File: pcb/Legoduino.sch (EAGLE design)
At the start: 91 parts, among them CON11 ISP-AVR, CON2 PIN(1+16)X3_DS, IC1 NCP3170ADR2G, IC2 RN-42, IC3 MIC5205-5.0YM5, IC4 ATMEGA2560-16AU, IC5 UG-2864HSWEG01_SPI, IC6 MIC5205-3.6YM5, IC7 MIC5205-3.3YM5, IC8 BD6221F-E2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

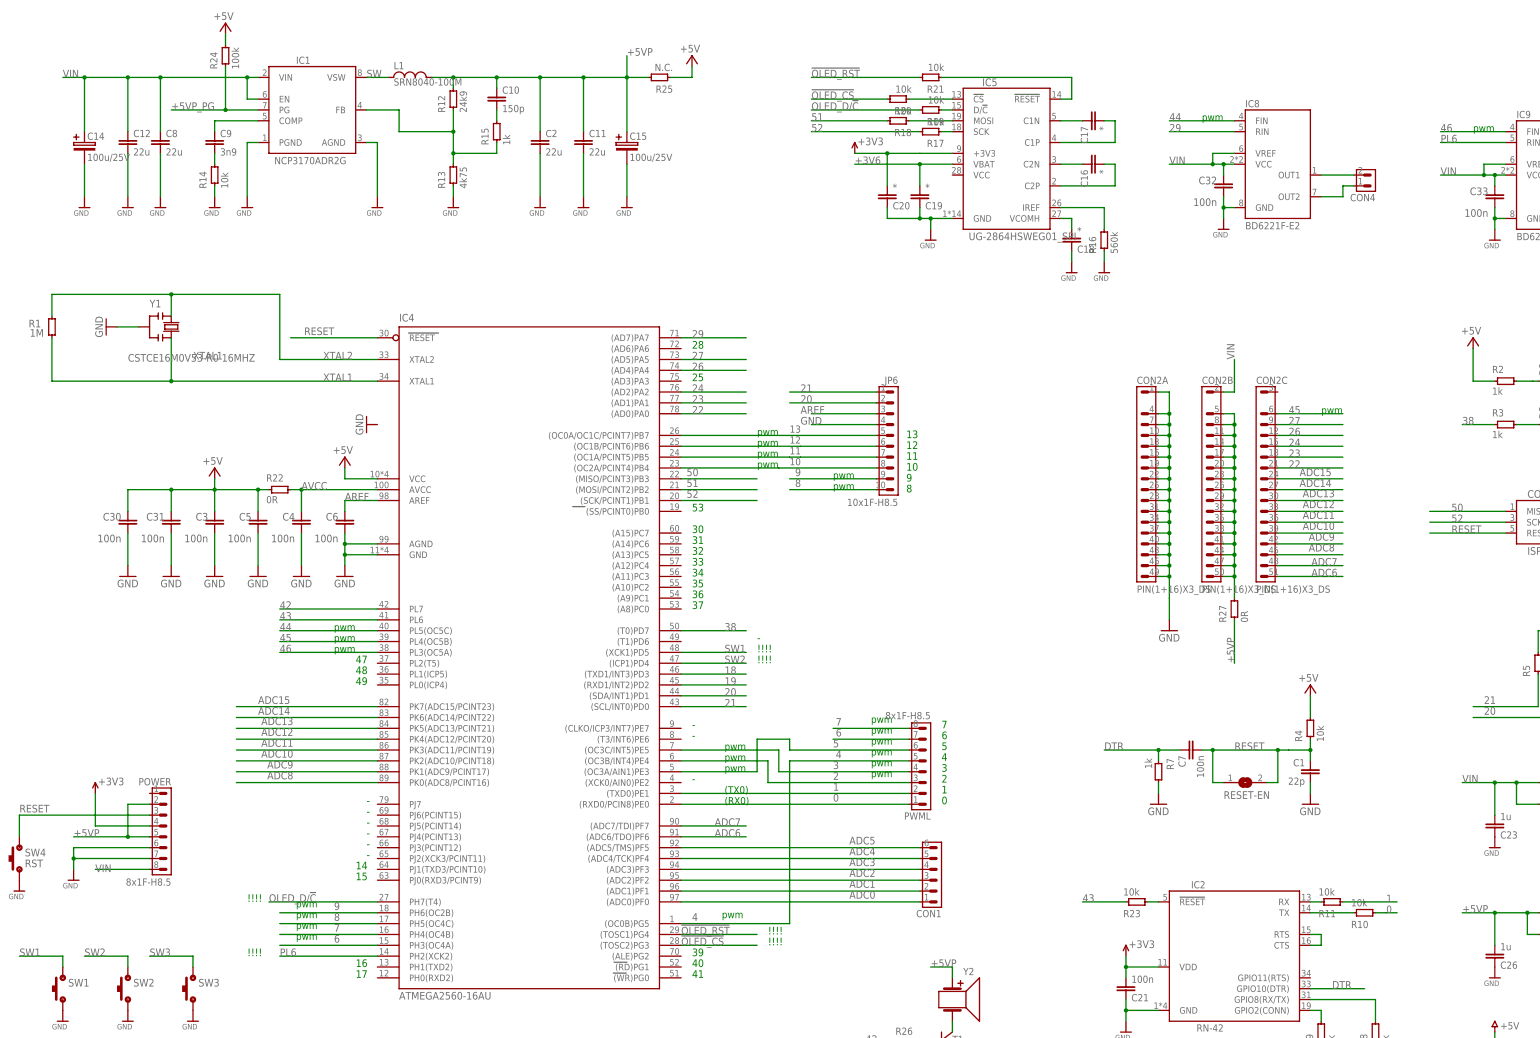
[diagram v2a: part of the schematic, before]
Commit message: Updated net names according to Arduino Mega pin numbers
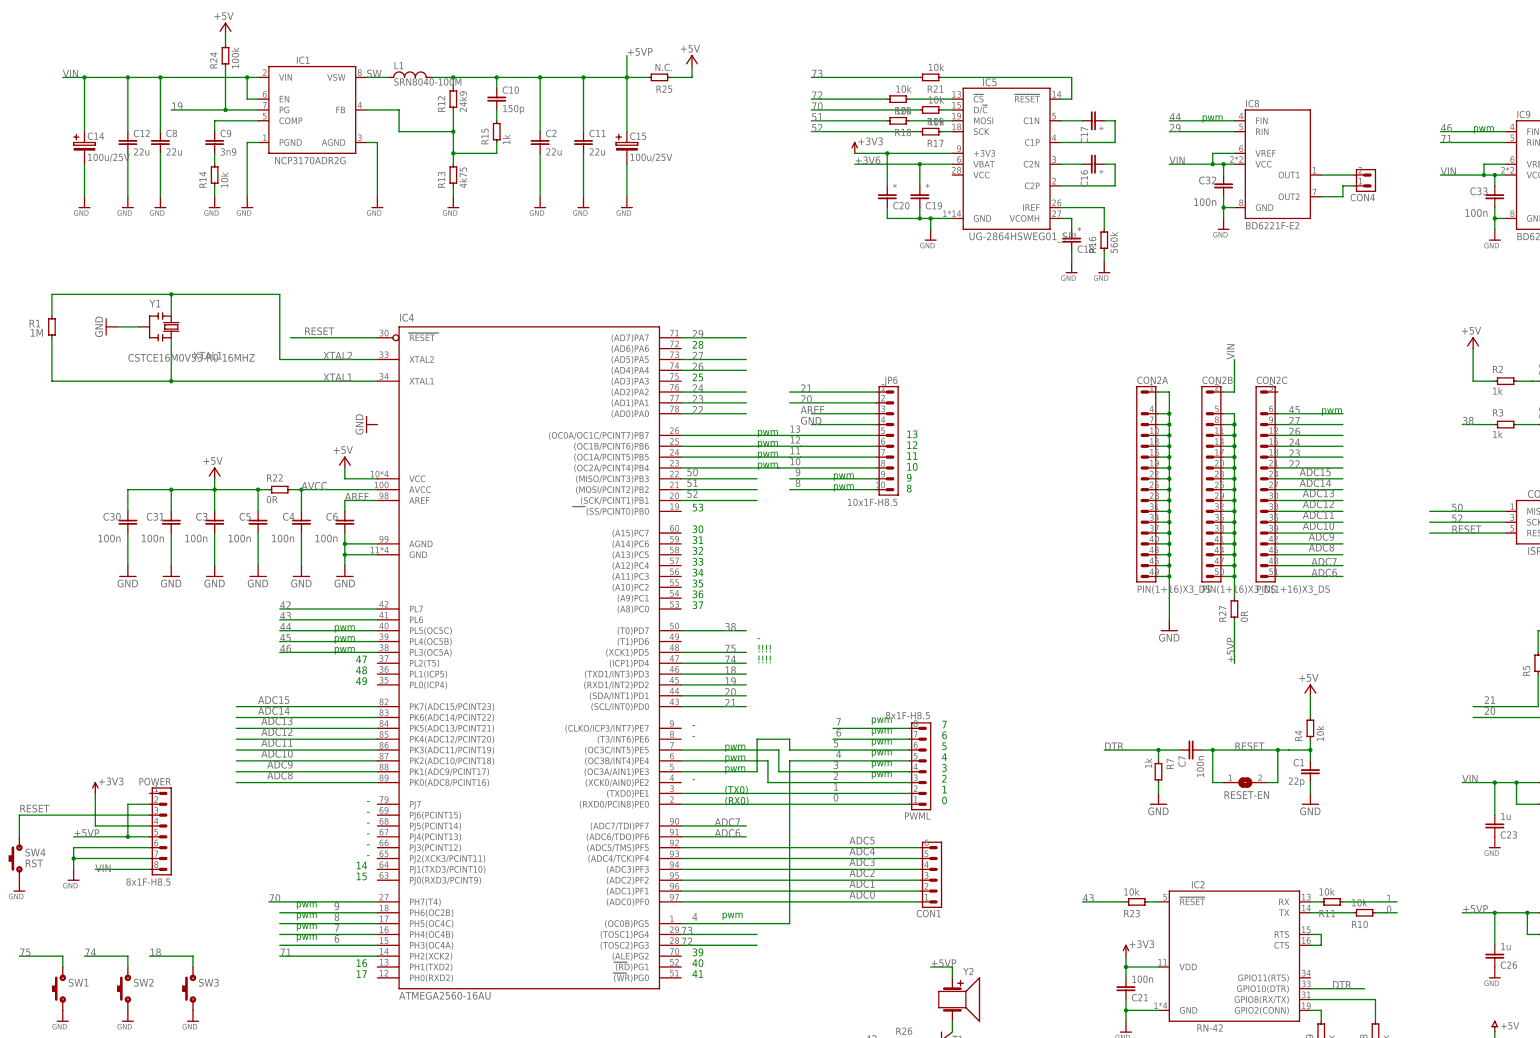
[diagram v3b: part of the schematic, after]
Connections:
- net !OLED_CS renamed 72
- net !OLED_RST renamed 73
- net OLED_D/!C renamed 70
- net PL6 renamed 71
- net SW1 renamed 75
- net SW2 renamed 74
- removed net +5VP_PG: IC1.PG, R24.1
- removed net SW3: SW3.1
- net 18: now also SW3.1
- net 19: now also IC1.PG, R24.1
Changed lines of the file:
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@@
 <text x="114.3" y="101.6" size="1.778" layer="91">14</text>
 <text x="114.3" y="99.06" size="1.778" layer="91">15</text>
-<text x="88.9" y="93.98" size="1.778" layer="91">!!!!</text>
-<text x="88.9" y="81.28" size="1.778" layer="91">!!!!</text>
 <text x="114.3" y="78.74" size="1.778" layer="91">16</text>
 <text x="114.3" y="76.2" size="1.778" layer="91">17</text>
 <text x="193.04" y="81.28" size="1.778" layer="91">39</text>
-<text x="210.82" y="86.36" size="1.778" layer="91">!!!!</text>
-<text x="210.82" y="83.82" size="1.778" layer="91">!!!!</text>
 <text x="193.04" y="78.74" size="1.778" layer="91">40</text>
 <text x="193.04" y="76.2" size="1.778" layer="91">41</text>
@@
 </segment>
 </net>
-<net name="OLED_D/!C" class="0">
+<net name="70" class="0">
 <segment>
 <label x="220.98" y="279.4" size="1.778" layer="95"/>
@@
 </segment>
 </net>
-<net name="!OLED_CS" class="0">
+<net name="72" class="0">
 <segment>
 <label x="220.98" y="281.94" size="1.778" layer="95"/>
@@
 </segment>
 </net>
-<net name="!OLED_RST" class="0">
+<net name="73" class="0">
 <segment>
 <pinref part="R21" gate="G$1" pin="2"/>
@@
 </segment>
 </net>
-<net name="+5VP_PG" class="0">
-<segment>
-<pinref part="IC1" gate="G$1" pin="PG"/>
-<wire x1="91.44" y1="279.4" x2="83.82" y2="279.4" width="0.1524" layer="91"/>
-<label x="71.12" y="279.4" size="1.778" layer="95"/>
-<pinref part="R24" gate="G$1" pin="1"/>
-<wire x1="83.82" y1="279.4" x2="71.12" y2="279.4" width="0.1524" layer="91"/>
-<wire x1="83.82" y1="289.56" x2="83.82" y2="279.4" width="0.1524" layer="91"/>
-<junction x="83.82" y="279.4"/>
-</segment>
-</net>
 <net name="N$29" class="0">
 <segment>
@@
 </segment>
 </net>
-<net name="PL6" class="0">
+<net name="71" class="0">
 <segment>
 <pinref part="IC4" gate="1" pin="PH2(XCK2)"/>
@@
 </segment>
 </net>
-<net name="SW1" class="0">
+<net name="75" class="0">
 <segment>
 <pinref part="SW1" gate="G$1" pin="1"/>
@@
 </segment>
 </net>
-<net name="SW2" class="0">
+<net name="74" class="0">
 <segment>
 <pinref part="SW2" gate="G$1" pin="1"/>
@@
 <label x="200.66" y="149.86" size="1.778" layer="95"/>
 <pinref part="IC4" gate="1" pin="(ICP1)PD4"/>
-</segment>
-</net>
-<net name="SW3" class="0">
-<segment>
-<pinref part="SW3" gate="G$1" pin="1"/>
-<wire x1="76.2" y1="78.74" x2="76.2" y2="81.28" width="0.1524" layer="91"/>
-<wire x1="76.2" y1="81.28" x2="66.04" y2="81.28" width="0.1524" layer="91"/>
-<label x="66.04" y="81.28" size="1.778" layer="95"/>
 </segment>
 </net>
@@
 <pinref part="IC4" gate="1" pin="(RXD1/INT2)PD2"/>
 </segment>
+<segment>
+<pinref part="IC1" gate="G$1" pin="PG"/>
+<wire x1="91.44" y1="279.4" x2="83.82" y2="279.4" width="0.1524" layer="91"/>
+<label x="71.12" y="279.4" size="1.778" layer="95"/>
+<pinref part="R24" gate="G$1" pin="1"/>
+<wire x1="83.82" y1="279.4" x2="71.12" y2="279.4" width="0.1524" layer="91"/>
+<wire x1="83.82" y1="289.56" x2="83.82" y2="279.4" width="0.1524" layer="91"/>
+<junction x="83.82" y="279.4"/>
+</segment>
 </net>
 <net name="18" class="0">
@@
 <pinref part="IC4" gate="1" pin="(TXD1/INT3)PD3"/>
 </segment>
-</net>
+<segment>
+<pinref part="SW3" gate="G$1" pin="1"/>
+<wire x1="76.2" y1="78.74" x2="76.2" y2="81.28" width="0.1524" layer="91"/>
+<wire x1="76.2" y1="81.28" x2="66.04" y2="81.28" width="0.1524" layer="91"/>
+<label x="66.04" y="81.28" size="1.778" layer="95"/>
+</segment>
+</net>

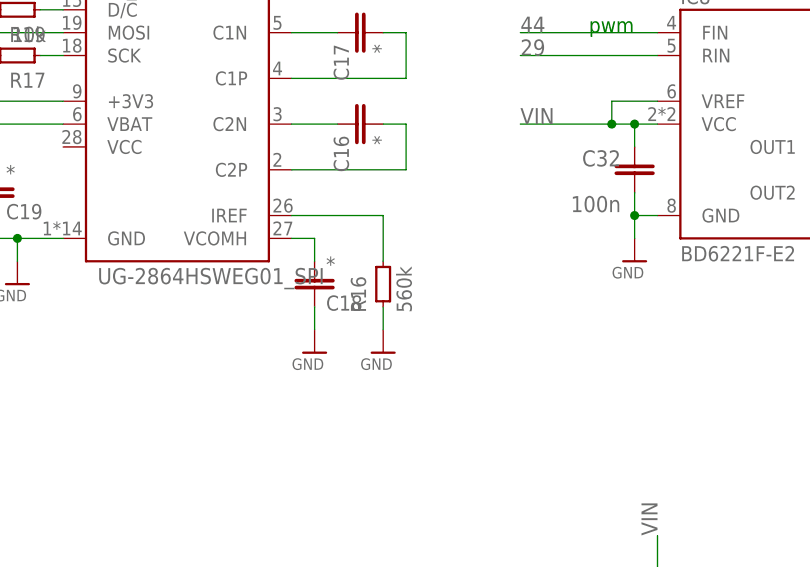
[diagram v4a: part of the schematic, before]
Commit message: R16 -> 390k. Closes #32.
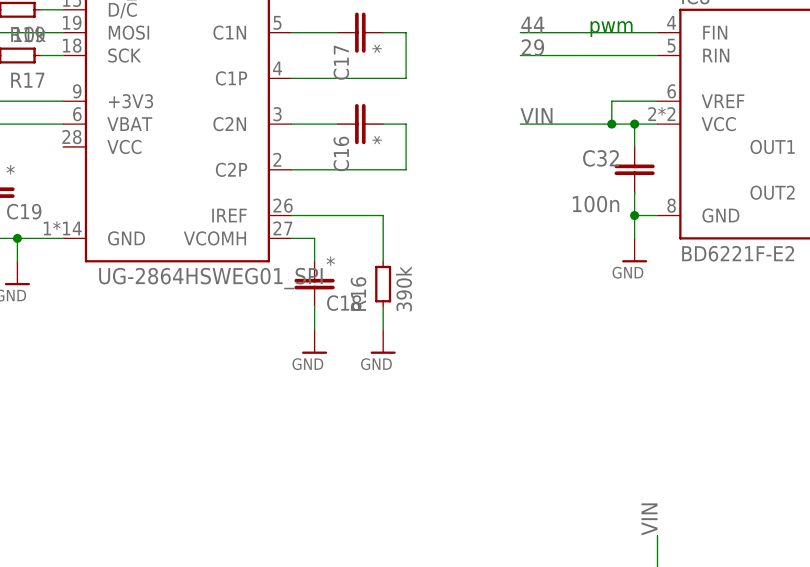
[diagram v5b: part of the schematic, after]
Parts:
- R16: value 560k -> 390k
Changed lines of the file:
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@@
 <part name="C18" library="PN_default" deviceset="C" device="0603" value="*"/>
 <part name="GND26" library="PN_default" deviceset="GND" device=""/>
-<part name="R16" library="PN_default" deviceset="R" device="0603" value="560k"/>
+<part name="R16" library="PN_default" deviceset="R" device="0603" value="390k"/>
 <part name="GND27" library="PN_default" deviceset="GND" device=""/>
 <part name="IC5" library="PN_opto" deviceset="UG-2864HSWEG01_SPI" device=""/>

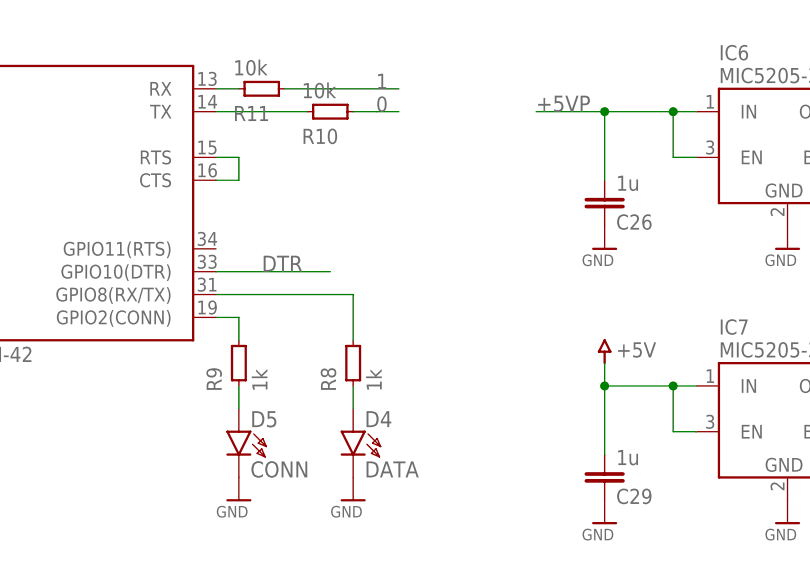
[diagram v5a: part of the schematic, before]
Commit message: Reverse DATA LED polarisation. Closes #15.
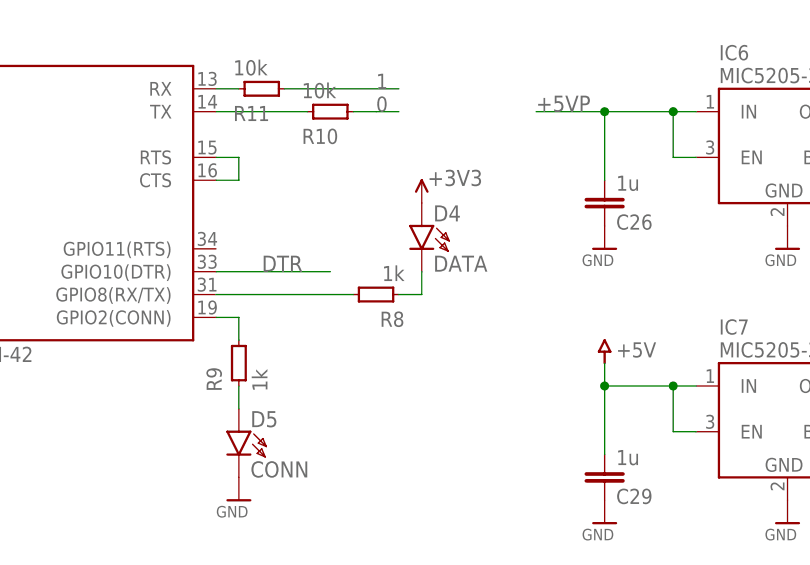
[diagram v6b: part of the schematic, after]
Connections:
- net +3V3: now also D4.A
- net GND: no longer D4.K
- net N$6: now also D4.K; no longer D4.A
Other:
- moved on the sheet: D4, R8
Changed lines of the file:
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@@
 <part name="D4" library="PN_default" deviceset="LED" device="0805" value="DATA"/>
 <part name="D5" library="PN_default" deviceset="LED" device="0805" value="CONN"/>
-<part name="GND3" library="PN_default" deviceset="GND" device=""/>
 <part name="GND4" library="PN_default" deviceset="GND" device=""/>
 <part name="IC4" library="PN_microcontrollers" deviceset="ATMEGA2560" device="AU" technology="-16"/>
@@
 <part name="P+6" library="supply1" deviceset="+5V" device=""/>
 <part name="R27" library="PN_default" deviceset="R" device="0805" value="0R"/>
+<part name="U$4" library="PN_default" deviceset="+3V3" device=""/>
 </parts>
 <sheets>
@@
 <instance part="R6" gate="G$1" x="398.78" y="149.86" rot="R90"/>
 <instance part="R7" gate="G$1" x="302.26" y="124.46" rot="R270"/>
-<instance part="R8" gate="G$1" x="353.06" y="63.5" rot="R90"/>
+<instance part="R8" gate="G$1" x="355.6" y="71.12" rot="R180"/>
 <instance part="R9" gate="G$1" x="340.36" y="63.5" rot="R90"/>
 <instance part="R10" gate="G$1" x="350.52" y="91.44" rot="MR180"/>
@@
 <instance part="D2" gate="G$1" x="396.24" y="215.9" rot="R90"/>
 <instance part="D3" gate="G$1" x="396.24" y="205.74" rot="R90"/>
-<instance part="D4" gate="G$1" x="353.06" y="53.34"/>
+<instance part="D4" gate="G$1" x="360.68" y="76.2"/>
 <instance part="D5" gate="G$1" x="340.36" y="53.34"/>
-<instance part="GND3" gate="G$1" x="353.06" y="48.26"/>
 <instance part="GND4" gate="G$1" x="340.36" y="48.26"/>
 <instance part="IC4" gate="1" x="154.94" y="149.86"/>
@@
 </instance>
 <instance part="R27" gate="G$1" x="320.04" y="162.56" rot="R90"/>
+<instance part="U$4" gate="G$1" x="360.68" y="83.82"/>
 </instances>
 <busses>
@@
 <pinref part="GND4" gate="G$1" pin="GND"/>
 <pinref part="D5" gate="G$1" pin="K"/>
-</segment>
-<segment>
-<pinref part="GND3" gate="G$1" pin="GND"/>
-<pinref part="D4" gate="G$1" pin="K"/>
 </segment>
 <segment>
@@
 <junction x="426.72" y="60.96"/>
 </segment>
+<segment>
+<pinref part="D4" gate="G$1" pin="A"/>
+<pinref part="U$4" gate="G$1" pin="+3V3"/>
+</segment>
 </net>
 <net name="20" class="0">
@@
 <segment>
 <pinref part="R8" gate="G$1" pin="2"/>
-<wire x1="353.06" y1="66.04" x2="353.06" y2="71.12" width="0.1524" layer="91"/>
 <wire x1="353.06" y1="71.12" x2="337.82" y2="71.12" width="0.1524" layer="91"/>
 <pinref part="IC2" gate="G$1" pin="GPIO8(RX/TX)"/>
-</segment>
-</net>
-<net name="N$6" class="0">
-<segment>
-<pinref part="D4" gate="G$1" pin="A"/>
-<pinref part="R8" gate="G$1" pin="1"/>
-<wire x1="353.06" y1="60.96" x2="353.06" y2="58.42" width="0.1524" layer="91"/>
 </segment>
 </net>
@@
 </segment>
 </net>
+<net name="N$6" class="0">
+<segment>
+<pinref part="R8" gate="G$1" pin="1"/>
+<pinref part="D4" gate="G$1" pin="K"/>
+<wire x1="358.14" y1="71.12" x2="360.68" y2="71.12" width="0.1524" layer="91"/>
+<wire x1="360.68" y1="71.12" x2="360.68" y2="73.66" width="0.1524" layer="91"/>
+</segment>
+</net>

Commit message: #20: Optimized pin assignment on arduino shield connector. PWM signals are now connected only to this lines, where PWM are on Arduino Uno board. 4 additional PWM are now connected to expansion connector. 2 are reserved to connect to OC transistors.
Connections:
- removed net 45: CON2C.2, IC4.PL4(OC5B)
- new net 25: CON2C.5, IC4.(OC3A/AIN1)PE3
- new net 28: CON2C.2, IC4.PL3(OC5A)
- new net OC_PWM1: IC4.PH3(OC4A)
- new net OC_PWM2: IC4.PL4(OC5B)
- net 10: now also IC4.(OC1B/PCINT6)PB6; no longer IC4.(OC2A/PCINT4)PB4
- net 11: now also IC4.(OC0A/OC1C/PCINT7)PB7; no longer IC4.(OC1A/PCINT5)PB5
- net 12: no longer IC4.(OC1B/PCINT6)PB6
- net 13: no longer IC4.(OC0A/OC1C/PCINT7)PB7
- net 2: now also IC4.PH0(RXD2); no longer IC4.(OC3B/INT4)PE4
- net 22: no longer CON2C.7
- net 23: now also CON2C.7; no longer CON2C.6
- net 24: now also CON2C.6, IC4.(OC0B)PG5; no longer CON2C.5, IC4.(AD2)PA2
- net 26: now also IC4.(OC3B/INT4)PE4; no longer IC4.(AD4)PA4
- net 27: now also IC4.(OC3C/INT5)PE5; no longer IC4.(AD5)PA5
- net 3: now also IC4.PH4(OC4B); no longer IC4.(OC3C/INT5)PE5
- net 4: now also IC4.PH1(TXD2); no longer IC4.(OC0B)PG5
- net 46: now also IC4.(OC2A/PCINT4)PB4; no longer IC4.PL3(OC5A)
- net 5: now also IC4.PH5(OC4C); no longer IC4.(OC3A/AIN1)PE3
- net 6: now also IC4.PH6(OC2B); no longer IC4.PH3(OC4A)
- net 7: now also IC4.PH2(XCK2); no longer IC4.PH4(OC4B)
- net 71: now also IC4.(SS/PCINT0)PB0; no longer IC4.PH2(XCK2)
- net 8: no longer IC4.PH5(OC4C)
- net 9: now also IC4.(OC1A/PCINT5)PB5; no longer IC4.PH6(OC2B)
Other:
- note removed: "16"
- note removed: "17"
- note removed: "53"
